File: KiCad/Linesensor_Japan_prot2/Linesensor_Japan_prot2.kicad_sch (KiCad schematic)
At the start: 153 parts, among them J1 Conn_01x04_Socket, J2 Conn_01x02_Socket, J3 Conn_01x09_Socket, J4 Conn_01x09_Socket, Q1 Q_Photo_NPN, Q10 Q_Photo_NPN, Q11 Q_Photo_NPN, Q12 Q_Photo_NPN, Q13 Q_Photo_NPN, Q14 Q_Photo_NPN, Q15 Q_Photo_NPN, Q16 Q_Photo_NPN, Q17 Q_Photo_NPN, Q18 Q_Photo_NPN, Q19 Q_Photo_NPN, Q2 Q_Photo_NPN, Q20 Q_Photo_NPN, Q21 Q_Photo_NPN, Q22 Q_Photo_NPN, Q23 Q_Photo_NPN, Q24 Q_Photo_NPN, Q25 Q_Photo_NPN, Q26 Q_Photo_NPN, Q27 Q_Photo_NPN, Q28 Q_Photo_NPN, Q29 Q_Photo_NPN, Q3 Q_Photo_NPN, Q30 Q_Photo_NPN, Q31 Q_Photo_NPN, Q32 Q_Photo_NPN, Q33 Q_NMOS, Q4 Q_Photo_NPN, Q5 Q_Photo_NPN, Q6 Q_Photo_NPN, Q7 Q_Photo_NPN, Q8 Q_Photo_NPN, Q9 Q_Photo_NPN, U1 CD74HC4067SM, U2 CD74HC4067SM

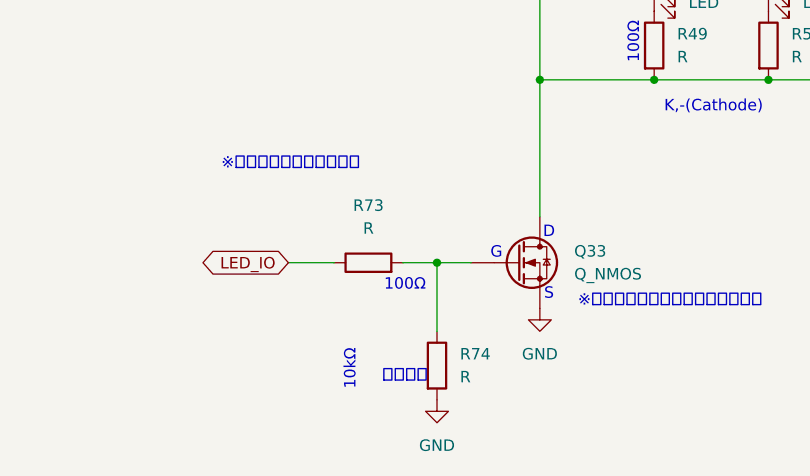
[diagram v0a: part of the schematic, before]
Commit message: 明日はラインセンサー簡易キャリブレーション
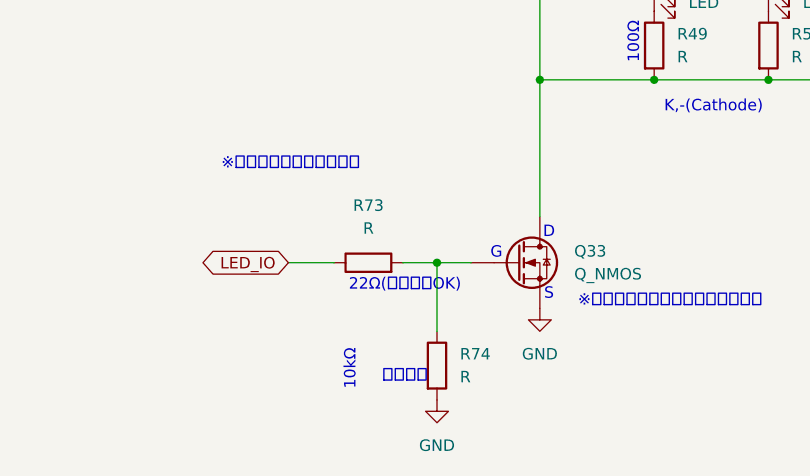
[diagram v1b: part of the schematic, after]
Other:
- note added: "22Ω(なくてもOK)"
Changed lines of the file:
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@@
 		)
 	)
-	(text "100Ω"
+	(text "22Ω(なくてもOK)"
 		(exclude_from_sim no)
 		(at 94.234 297.18 0)

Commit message: [悲報]103と101間違える
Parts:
- added Q34: Q_NMOS, seeeduino:TO-251-3-1EP_Horizontal_TabDown_EDITED, symbol Device:Q_NMOS
- added R65, R66, R67, R68: R, Resistor_THT:R_Axial_DIN0309_L9.0mm_D3.2mm_P12.70mm_Horizontal, symbol Device:R
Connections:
- net GND: now also Q34.2 (S), R66.2
- net LED_IO: now also R65.1
- new net: Q34.1 (G), R65.2, R66.1
- new net: Q34.3 (D), R67.1, R68.1
- new net: R67.2, R68.2
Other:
- note added: "22Ω"
- note added: "MOSFET中央の穴 Drain =LED K"
